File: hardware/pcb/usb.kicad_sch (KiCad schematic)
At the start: 4 parts, among them U5 CP2102N-A02-GQFN28R

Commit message: Pack the hw_v1 board to 36.2 x 28 mm and correct the 3D models.
The LSM6 body is a 3.0 x 2.5 x 0.83 mm box in KiCad VRML units, and the other vendor models are rotated so they stand on their lands. Skin sensors sit in one bottom cluster with the electrode pads around them, bypass parts are packed next to their ICs outside the antenna keep-out, and the schematic frames clear the title block.

Co-authored-by: Riyu-D1 <Riyu-D1@users.noreply.github.com>
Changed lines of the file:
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@@
 		(instances
 			(project "vitalq_hw_v1"
-				(path "/3a03f3a2-f664-49ab-a6e3-0e34faafa582/5dacf7e4-5358-490a-93f6-d5de92dddf35"
+				(path "/6fcf6b13-4a8e-4f25-a8b9-d34cb547168d/2b2375ea-536a-4b8a-804e-13c143c23fea"
 					(reference "U5")
 					(unit 1)
@@
 		(instances
 			(project "vitalq_hw_v1"
-				(path "/3a03f3a2-f664-49ab-a6e3-0e34faafa582/5dacf7e4-5358-490a-93f6-d5de92dddf35"
+				(path "/6fcf6b13-4a8e-4f25-a8b9-d34cb547168d/2b2375ea-536a-4b8a-804e-13c143c23fea"
 					(reference "#PWR022")
 					(unit 1)
@@
 		(instances
 			(project "vitalq_hw_v1"
-				(path "/3a03f3a2-f664-49ab-a6e3-0e34faafa582/5dacf7e4-5358-490a-93f6-d5de92dddf35"
+				(path "/6fcf6b13-4a8e-4f25-a8b9-d34cb547168d/2b2375ea-536a-4b8a-804e-13c143c23fea"
 					(reference "#PWR023")
 					(unit 1)
@@
 		(instances
 			(project "vitalq_hw_v1"
-				(path "/3a03f3a2-f664-49ab-a6e3-0e34faafa582/5dacf7e4-5358-490a-93f6-d5de92dddf35"
+				(path "/6fcf6b13-4a8e-4f25-a8b9-d34cb547168d/2b2375ea-536a-4b8a-804e-13c143c23fea"
 					(reference "C9")
 					(unit 1)
@@
 		(instances
 			(project "vitalq_hw_v1"
-				(path "/3a03f3a2-f664-49ab-a6e3-0e34faafa582/5dacf7e4-5358-490a-93f6-d5de92dddf35"
+				(path "/6fcf6b13-4a8e-4f25-a8b9-d34cb547168d/2b2375ea-536a-4b8a-804e-13c143c23fea"
 					(reference "#PWR024")
 					(unit 1)
@@
 		(instances
 			(project "vitalq_hw_v1"
-				(path "/3a03f3a2-f664-49ab-a6e3-0e34faafa582/5dacf7e4-5358-490a-93f6-d5de92dddf35"
+				(path "/6fcf6b13-4a8e-4f25-a8b9-d34cb547168d/2b2375ea-536a-4b8a-804e-13c143c23fea"
 					(reference "C10")
 					(unit 1)
@@
 		(instances
 			(project "vitalq_hw_v1"
-				(path "/3a03f3a2-f664-49ab-a6e3-0e34faafa582/5dacf7e4-5358-490a-93f6-d5de92dddf35"
+				(path "/6fcf6b13-4a8e-4f25-a8b9-d34cb547168d/2b2375ea-536a-4b8a-804e-13c143c23fea"
 					(reference "#PWR025")
 					(unit 1)
@@
 		(instances
 			(project "vitalq_hw_v1"
-				(path "/3a03f3a2-f664-49ab-a6e3-0e34faafa582/5dacf7e4-5358-490a-93f6-d5de92dddf35"
+				(path "/6fcf6b13-4a8e-4f25-a8b9-d34cb547168d/2b2375ea-536a-4b8a-804e-13c143c23fea"
 					(reference "#PWR026")
 					(unit 1)
@@
 		(instances
 			(project "vitalq_hw_v1"
-				(path "/3a03f3a2-f664-49ab-a6e3-0e34faafa582/5dacf7e4-5358-490a-93f6-d5de92dddf35"
+				(path "/6fcf6b13-4a8e-4f25-a8b9-d34cb547168d/2b2375ea-536a-4b8a-804e-13c143c23fea"
 					(reference "R4")
 					(unit 1)
@@
 		(instances
 			(project "vitalq_hw_v1"
-				(path "/3a03f3a2-f664-49ab-a6e3-0e34faafa582/5dacf7e4-5358-490a-93f6-d5de92dddf35"
+				(path "/6fcf6b13-4a8e-4f25-a8b9-d34cb547168d/2b2375ea-536a-4b8a-804e-13c143c23fea"
 					(reference "#FLG027")
 					(unit 1)
@@
 	)
 	(rectangle
-		(start 12.0 18.0)
+		(start 12.0 40.0)
 		(end 400.0 250.0)
 		(stroke (width 0.4) (type dash))

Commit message: Seat the QFN models and drop passives the datasheets do not require.
The ADS1292R STEP is already Z-up, so the extra X rotation stood the
4x4x1 mm body on edge. Remove TP1, TP2, C5, C12, C17, C31 and R4, add
the 1 uF AVDD bulk capacitor, and shorten the outline to 36.2 x 27.8 mm.

Co-authored-by: Riyu-D1 <Riyu-D1@users.noreply.github.com>
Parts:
- removed R4: 1k, Resistor_SMD:R_0402_1005Metric, symbol vitalq:R
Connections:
- net CP_RST: no longer names the net of U5.9 (~{RST})
- no-connect marks 14 -> 15
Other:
- note added: "Decoupling"
- note added: "Unused inputs ~CTS, ~DSR, ~DCD and ~RI/CLK are tied to VDD_CP2102. ~RSTb is open."
- note removed: "Decoupling and ~RST"
- note removed: "Unused inputs ~CTS, ~DSR, ~DCD and ~RI/CLK are tied to VDD_CP2102."
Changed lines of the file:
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@@
 		(instances
 			(project "vitalq_hw_v1"
-				(path "/6fcf6b13-4a8e-4f25-a8b9-d34cb547168d/2b2375ea-536a-4b8a-804e-13c143c23fea"
+				(path "/1ff916b4-4a8a-459e-a757-b43de2b086a6/b972c2f9-af0d-435a-a598-bd016b260e0a"
 					(reference "U5")
 					(unit 1)
@@
 		(on_board no)
 		(dnp no)
-		(property "Reference" "#PWR022"
+		(property "Reference" "#PWR020"
 			(at 179.07 84.56 0)
 			(effects (font (size 1.27 1.27)) (hide yes))
@@
 		(instances
 			(project "vitalq_hw_v1"
-				(path "/6fcf6b13-4a8e-4f25-a8b9-d34cb547168d/2b2375ea-536a-4b8a-804e-13c143c23fea"
-					(reference "#PWR022")
+				(path "/1ff916b4-4a8a-459e-a757-b43de2b086a6/b972c2f9-af0d-435a-a598-bd016b260e0a"
+					(reference "#PWR020")
 					(unit 1)
 				)
@@
 		(on_board no)
 		(dnp no)
-		(property "Reference" "#PWR023"
+		(property "Reference" "#PWR021"
 			(at 199.39 167.11 0)
 			(effects (font (size 1.27 1.27)) (hide yes))
@@
 		(instances
 			(project "vitalq_hw_v1"
-				(path "/6fcf6b13-4a8e-4f25-a8b9-d34cb547168d/2b2375ea-536a-4b8a-804e-13c143c23fea"
-					(reference "#PWR023")
+				(path "/1ff916b4-4a8a-459e-a757-b43de2b086a6/b972c2f9-af0d-435a-a598-bd016b260e0a"
+					(reference "#PWR021")
 					(unit 1)
 				)
@@
 		(instances
 			(project "vitalq_hw_v1"
-				(path "/6fcf6b13-4a8e-4f25-a8b9-d34cb547168d/2b2375ea-536a-4b8a-804e-13c143c23fea"
+				(path "/1ff916b4-4a8a-459e-a757-b43de2b086a6/b972c2f9-af0d-435a-a598-bd016b260e0a"
 					(reference "C9")
 					(unit 1)
@@
 		(on_board no)
 		(dnp no)
-		(property "Reference" "#PWR024"
+		(property "Reference" "#PWR022"
 			(at 54.61 75.67 0)
 			(effects (font (size 1.27 1.27)) (hide yes))
@@
 		(instances
 			(project "vitalq_hw_v1"
-				(path "/6fcf6b13-4a8e-4f25-a8b9-d34cb547168d/2b2375ea-536a-4b8a-804e-13c143c23fea"
-					(reference "#PWR024")
+				(path "/1ff916b4-4a8a-459e-a757-b43de2b086a6/b972c2f9-af0d-435a-a598-bd016b260e0a"
+					(reference "#PWR022")
 					(unit 1)
 				)
@@
 		(instances
 			(project "vitalq_hw_v1"
-				(path "/6fcf6b13-4a8e-4f25-a8b9-d34cb547168d/2b2375ea-536a-4b8a-804e-13c143c23fea"
+				(path "/1ff916b4-4a8a-459e-a757-b43de2b086a6/b972c2f9-af0d-435a-a598-bd016b260e0a"
 					(reference "C10")
 					(unit 1)
@@
 		(on_board no)
 		(dnp no)
-		(property "Reference" "#PWR025"
+		(property "Reference" "#PWR023"
 			(at 77.47 60.43 0)
 			(effects (font (size 1.27 1.27)) (hide yes))
@@
 		(instances
 			(project "vitalq_hw_v1"
-				(path "/6fcf6b13-4a8e-4f25-a8b9-d34cb547168d/2b2375ea-536a-4b8a-804e-13c143c23fea"
-					(reference "#PWR025")
+				(path "/1ff916b4-4a8a-459e-a757-b43de2b086a6/b972c2f9-af0d-435a-a598-bd016b260e0a"
+					(reference "#PWR023")
 					(unit 1)
 				)
@@
 		(on_board no)
 		(dnp no)
-		(property "Reference" "#PWR026"
+		(property "Reference" "#PWR024"
 			(at 77.47 75.67 0)
 			(effects (font (size 1.27 1.27)) (hide yes))
@@
 		(instances
 			(project "vitalq_hw_v1"
-				(path "/6fcf6b13-4a8e-4f25-a8b9-d34cb547168d/2b2375ea-536a-4b8a-804e-13c143c23fea"
-					(reference "#PWR026")
-					(unit 1)
-				)
-			)
-		)
-	)
-	(symbol
-		(lib_id "vitalq:R")
-		(at 101.6 69.85 0)
-		(unit 1)
-		(exclude_from_sim no)
-		(in_bom yes)
-		(on_board yes)
-		(dnp no)
-		(property "Reference" "R4"
-			(at 106.5 68.6 0)
-			(effects (font (size 1.27 1.27)))
-		)
-		(property "Value" "1k"
-			(at 106.5 71.6 0)
-			(effects (font (size 1.27 1.27)))
-		)
-		(property "Footprint" "Resistor_SMD:R_0402_1005Metric"
-			(at 101.6 69.85 0)
-			(effects (font (size 1.27 1.27)) (hide yes))
-		)
-		(property "Datasheet" ""
-			(at 101.6 69.85 0)
-			(effects (font (size 1.27 1.27)) (hide yes))
-		)
-		(pin "1")
-		(pin "2")
-		(instances
-			(project "vitalq_hw_v1"
-				(path "/6fcf6b13-4a8e-4f25-a8b9-d34cb547168d/2b2375ea-536a-4b8a-804e-13c143c23fea"
-					(reference "R4")
+				(path "/1ff916b4-4a8a-459e-a757-b43de2b086a6/b972c2f9-af0d-435a-a598-bd016b260e0a"
+					(reference "#PWR024")
 					(unit 1)
 				)
@@
 		(on_board no)
 		(dnp no)
-		(property "Reference" "#FLG027"
+		(property "Reference" "#FLG025"
 			(at 142.24 60.43 0)
 			(effects (font (size 1.27 1.27)) (hide yes))
@@
 		(instances
 			(project "vitalq_hw_v1"
-				(path "/6fcf6b13-4a8e-4f25-a8b9-d34cb547168d/2b2375ea-536a-4b8a-804e-13c143c23fea"
-					(reference "#FLG027")
+				(path "/1ff916b4-4a8a-459e-a757-b43de2b086a6/b972c2f9-af0d-435a-a598-bd016b260e0a"
+					(reference "#FLG025")
 					(unit 1)
 				)
@@
 		)
 	)
-	(wire
-		(pts
-			(xy 186.69 101.6)
-			(xy 177.8 101.6)
-		)
-		(stroke (width 0) (type default))
-	)
-	(global_label "CP_RST"
-		(shape passive)
-		(at 177.8 101.6 180)
-		(effects (font (size 1.27 1.27)) (justify right))
-		(property "Intersheetrefs" "${INTERSHEET_REFS}"
-			(at 177.8 101.6 0)
-			(effects (font (size 1.27 1.27)) (hide yes))
-		)
-	)
 	(junction (at 199.39 162.56) (diameter 0) (color 0 0 0 0))
 	(wire
@@
 		)
 	)
+	(no_connect (at 186.69 101.6))
 	(no_connect (at 212.09 106.68))
 	(no_connect (at 212.09 114.3))
@@
 	(no_connect (at 212.09 154.94))
 	(no_connect (at 212.09 157.48))
-	(text "Decoupling and ~RST"
+	(text "Decoupling"
 		(exclude_from_sim no)
 		(at 40.0 48.0 0)
@@
 		(stroke (width 0) (type default))
 	)
-	(wire
-		(pts
-			(xy 101.6 66.04)
-			(xy 101.6 62.23)
-		)
-		(stroke (width 0) (type default))
-	)
-	(global_label "VDD_CP2102"
-		(shape passive)
-		(at 101.6 62.23 270)
-		(effects (font (size 1.27 1.27)) (justify left))
-		(property "Intersheetrefs" "${INTERSHEET_REFS}"
-			(at 101.6 62.23 0)
-			(effects (font (size 1.27 1.27)) (hide yes))
-		)
-	)
-	(wire
-		(pts
-			(xy 101.6 73.66)
-			(xy 101.6 77.47)
-		)
-		(stroke (width 0) (type default))
-	)
-	(global_label "CP_RST"
-		(shape passive)
-		(at 101.6 77.47 90)
-		(effects (font (size 1.27 1.27)) (justify right))
-		(property "Intersheetrefs" "${INTERSHEET_REFS}"
-			(at 101.6 77.47 0)
-			(effects (font (size 1.27 1.27)) (hide yes))
-		)
-	)
 	(global_label "VDD_CP2102"
 		(shape passive)
@@
 		(effects (font (size 1.4 1.4)) (justify left bottom))
 	)
-	(text "Unused inputs ~CTS, ~DSR, ~DCD and ~RI/CLK are tied to VDD_CP2102."
+	(text "Unused inputs ~CTS, ~DSR, ~DCD and ~RI/CLK are tied to VDD_CP2102. ~RSTb is open."
 		(exclude_from_sim no)
 		(at 40.0 106.0 0)

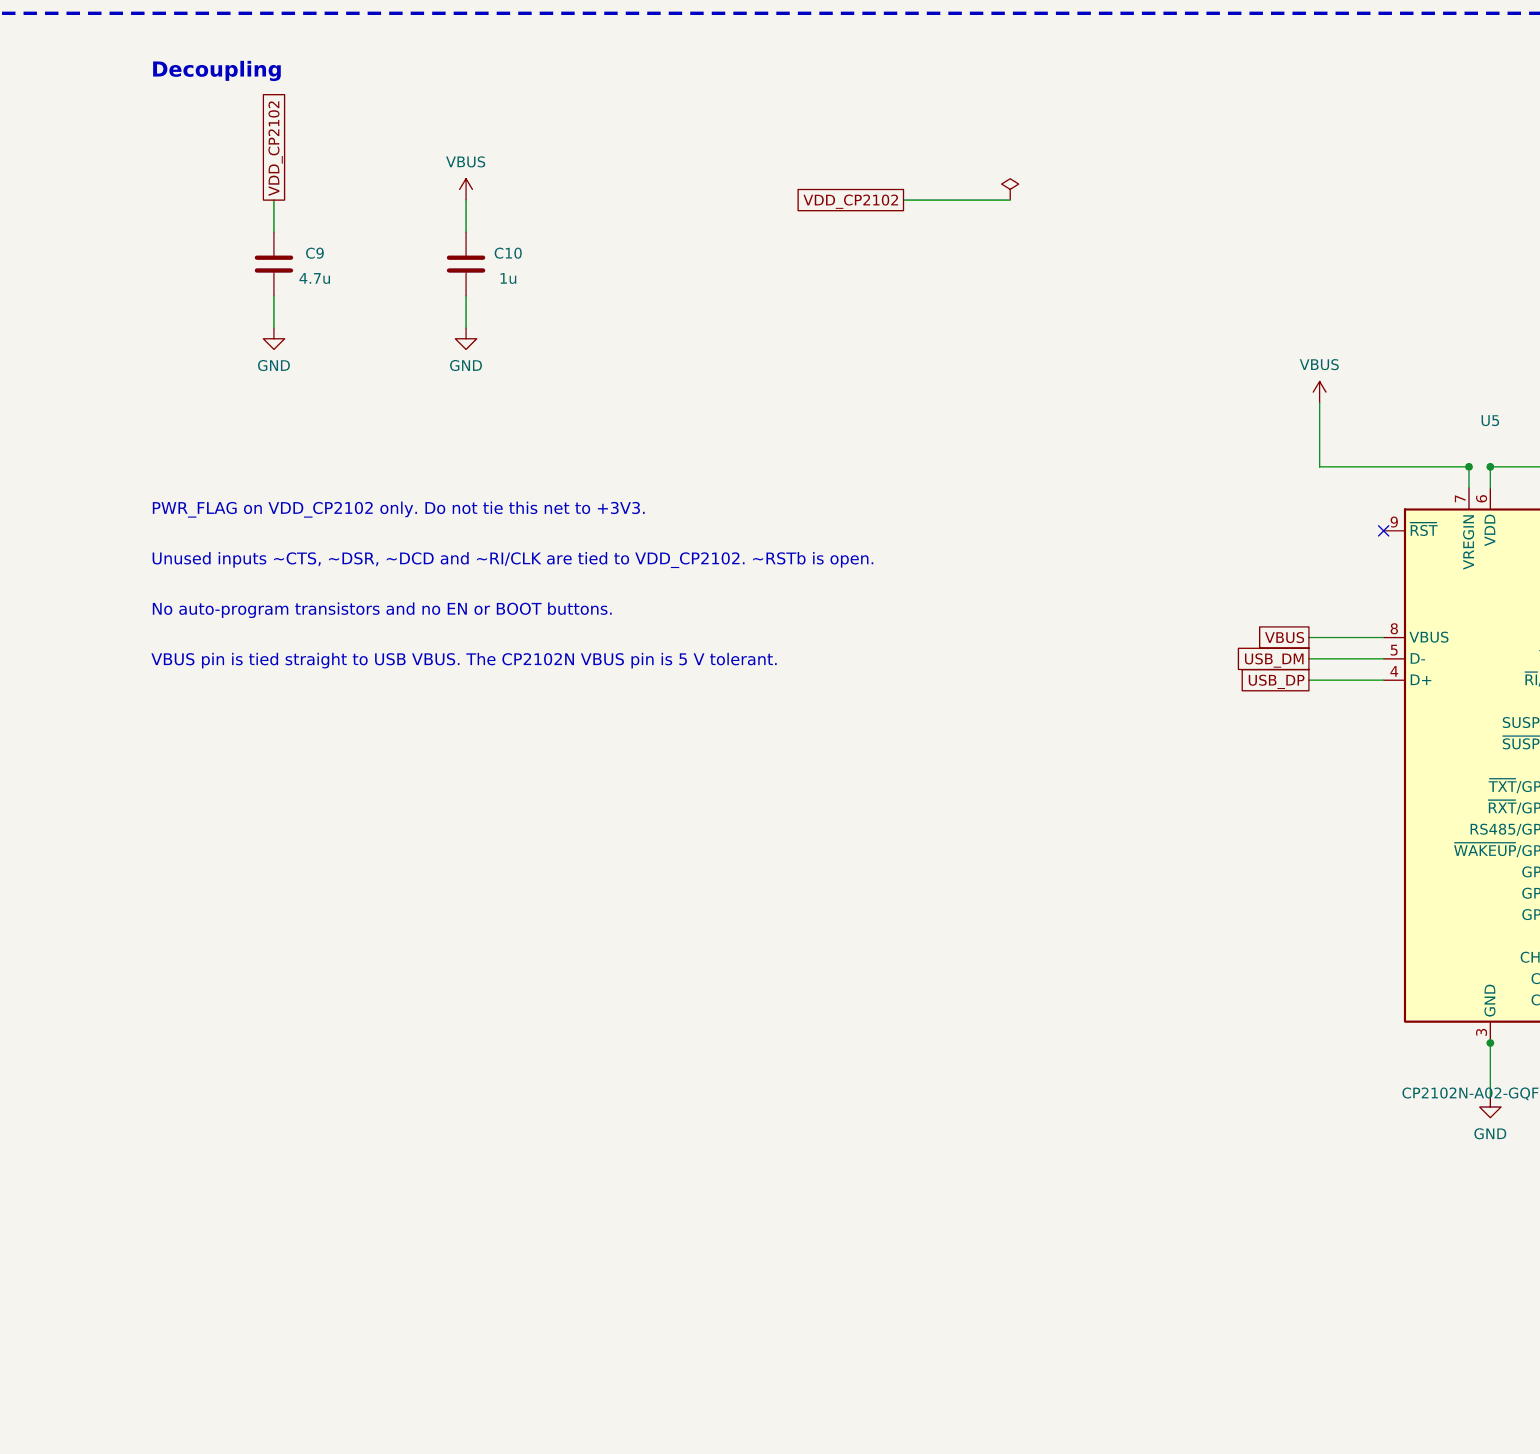
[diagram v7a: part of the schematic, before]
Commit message: Fix the CP2102N sense pin and add electrode creepage slots.
The USB sense pin was tied to 5 V. It now uses the datasheet divider, with the reset pull-up and the missing 100 nF bypasses. The TMP117 alert has its pull-up. Three slots raise creepage between the pulse resistors to 4.0 mm on a 1.6 mm board. Nothing was removed.

Co-authored-by: Riyu-D1 <Riyu-D1@users.noreply.github.com>
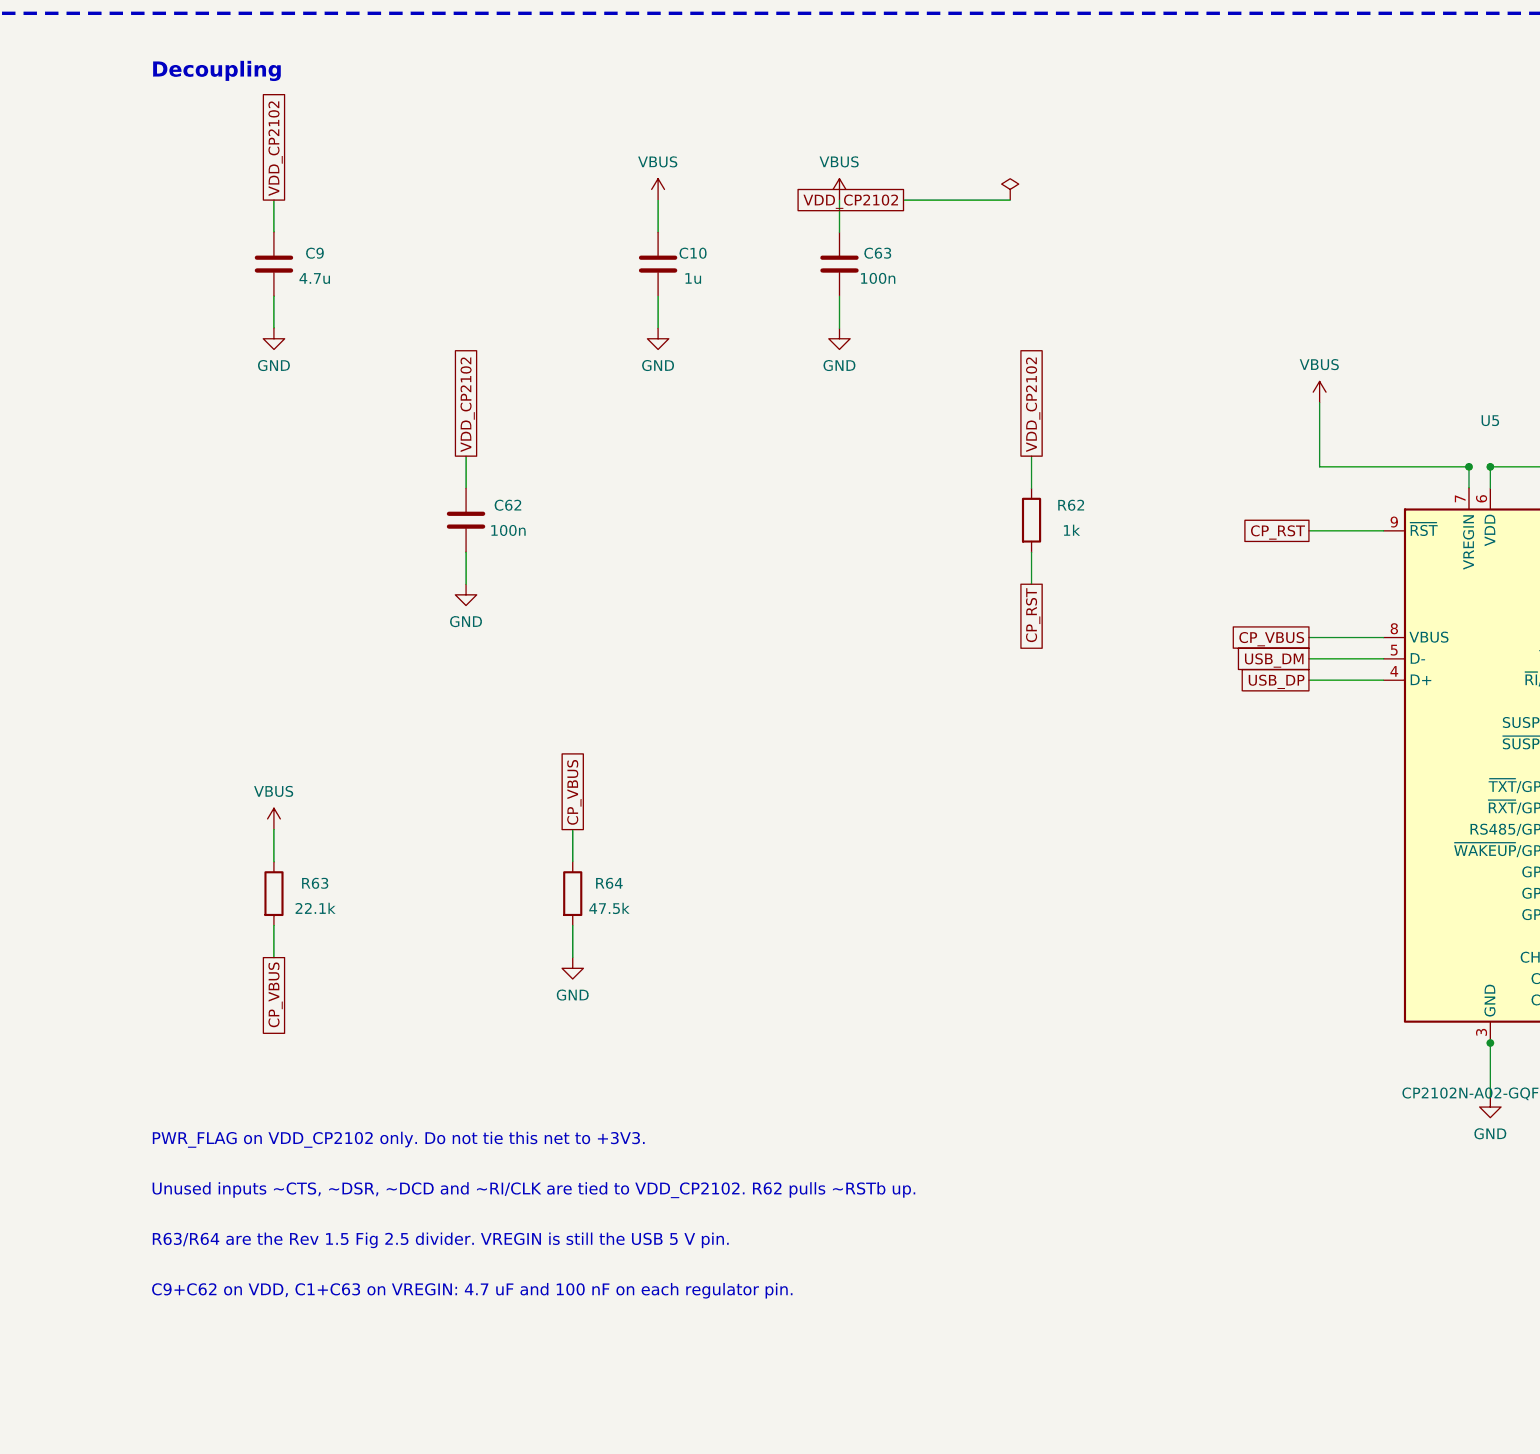
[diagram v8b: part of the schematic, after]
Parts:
- added C62, C63: 100n, Capacitor_SMD:C_0402_1005Metric, symbol vitalq:C
- added R62: 1k, Resistor_SMD:R_0402_1005Metric, symbol vitalq:R
- added R63: 22.1k, Resistor_SMD:R_0402_1005Metric, symbol vitalq:R
- added R64: 47.5k, Resistor_SMD:R_0402_1005Metric, symbol vitalq:R
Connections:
- net GND: now also C62.2, C63.2, R64.2
- net VBUS: now also C63.1, R63.1; no longer U5.8 (VBUS)
- net VDD_CP2102: now also C62.1, R62.1
- net CP_RST: now reaches U5.9 (~{RST})
- net CP_RST: now also R62.2
- new net CP_VBUS: R63.2, R64.1, U5.8 (VBUS)
- no-connect marks 15 -> 14
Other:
- note added: "C9+C62 on VDD, C1+C63 on VREGIN: 4.7 uF and 100 nF on each regulator pin."
- note added: "R63/R64 are the Rev 1.5 Fig 2.5 divider. VREGIN is still the USB 5 V pin."
- note added: "Unused inputs ~CTS, ~DSR, ~DCD and ~RI/CLK are tied to VDD_CP2102. R62 pulls ~RSTb up."
- note removed: "No auto-program transistors and no EN or BOOT buttons."
- note removed: "Unused inputs ~CTS, ~DSR, ~DCD and ~RI/CLK are tied to VDD_CP2102. ~RSTb is open."
- note removed: "VBUS pin is tied straight to USB VBUS. The CP2102N VBUS pin is 5 V tolerant."
